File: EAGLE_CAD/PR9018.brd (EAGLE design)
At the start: 70 x 70 mm, 72 parts

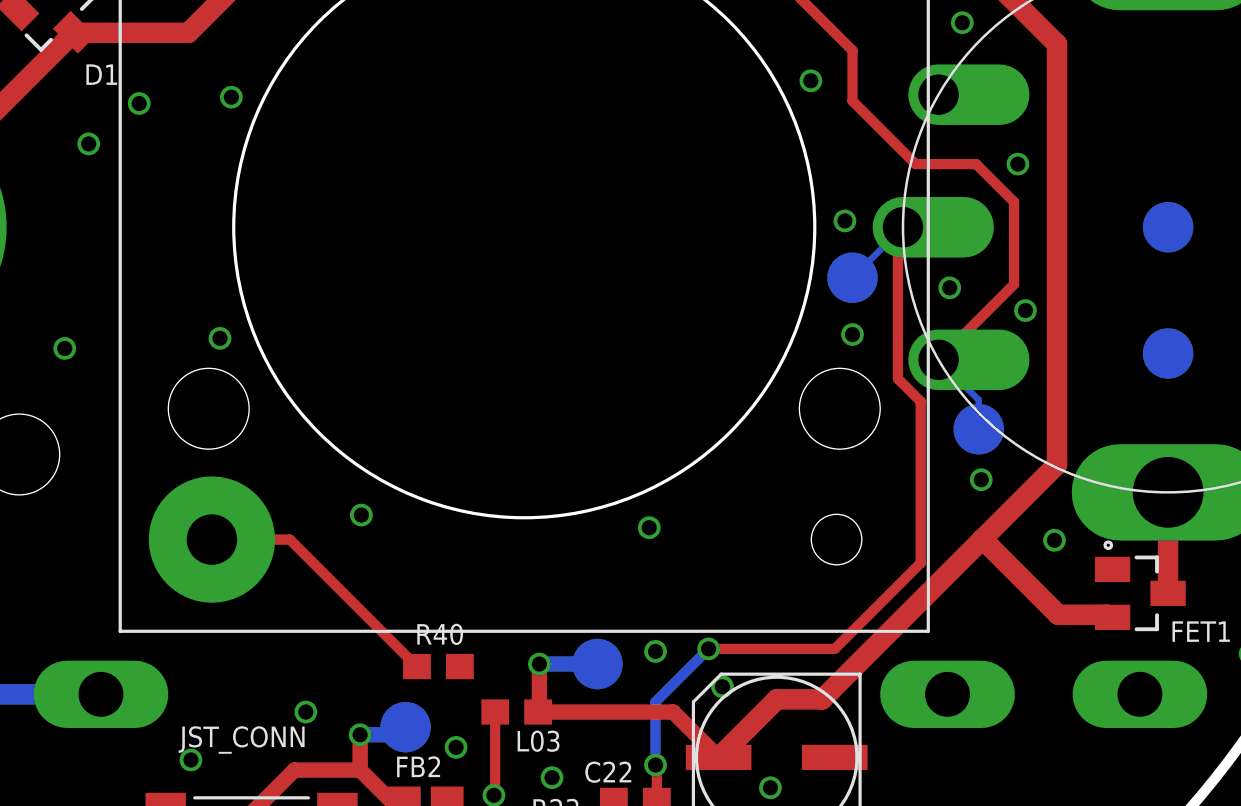
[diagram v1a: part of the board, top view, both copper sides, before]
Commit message: mostly speaker change
added big slot for wires
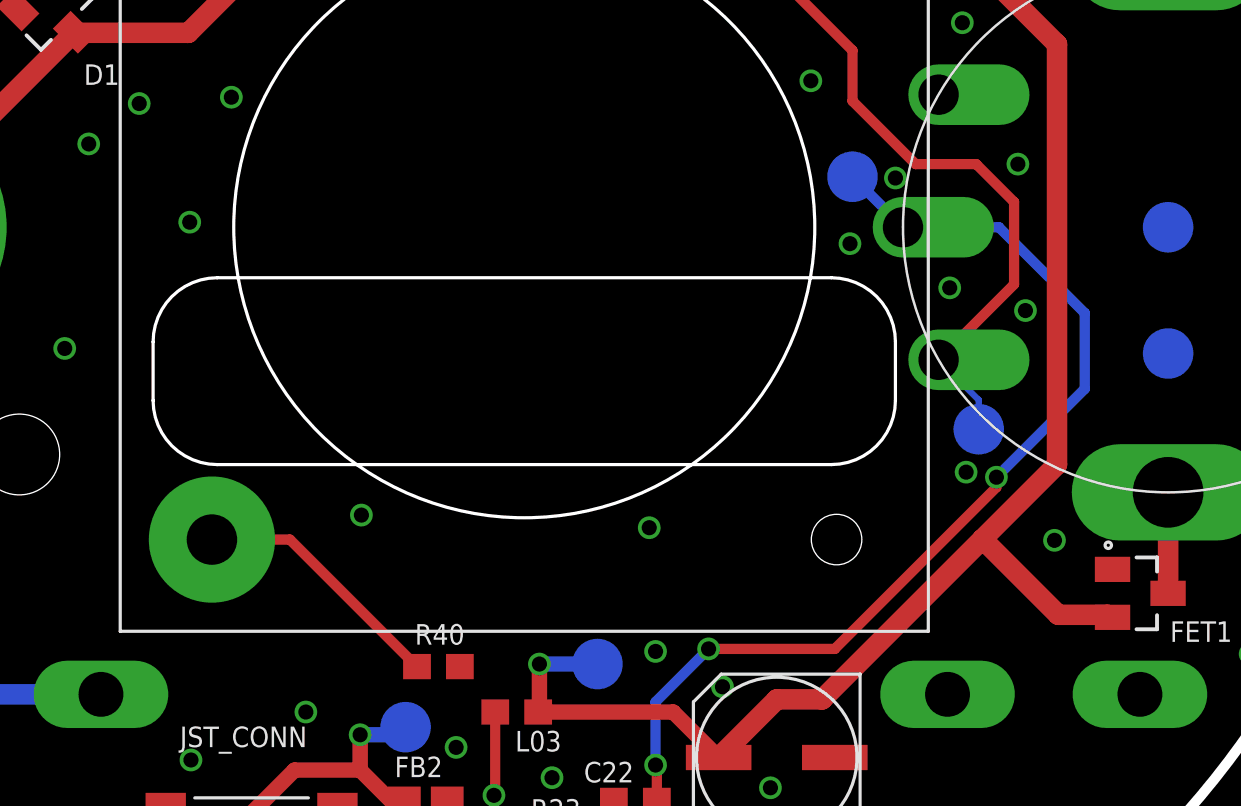
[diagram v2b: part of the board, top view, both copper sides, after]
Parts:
- moved TP17 4.00 mm to (48.0, 37.0)
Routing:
- net A_OUT: track 33.3 -> 40.7 mm, vias 2 -> 3
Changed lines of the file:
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@@
 <?xml version="1.0" encoding="utf-8"?>
 <!DOCTYPE eagle SYSTEM "eagle.dtd">
-<eagle version="6.6.0">
+<eagle version="7.2.0">
 <drawing>
 <settings>
@@
 <pass name="Default">
 <param name="RoutingGrid" value="50mil"/>
+<param name="AutoGrid" value="1"/>
+<param name="Efforts" value="0"/>
+<param name="TopRouterVariant" value="1"/>
 <param name="tpViaShape" value="round"/>
 <param name="PrefDir.1" value="|"/>
@@
 <attribute name="MFG_PN" value="DNP" x="53" y="27" size="1.778" layer="28" rot="MR0" display="off"/>
 </element>
-<element name="TP17" library="PR_Parts_Library" package="TP20R" value="" x="48" y="33" smashed="yes" rot="MR0">
-<attribute name="NAME" x="49" y="30.75" size="0.8128" layer="26" font="vector" ratio="16" rot="MR0"/>
-<attribute name="VALUE" x="48.762" y="31.984" size="0.0254" layer="28" rot="MR0"/>
-<attribute name="MFG_PN" value="DNP" x="48" y="33" size="1.778" layer="28" rot="MR0" display="off"/>
+<element name="TP17" library="PR_Parts_Library" package="TP20R" value="" x="48" y="37" smashed="yes" rot="MR0">
+<attribute name="NAME" x="49" y="34.75" size="0.8128" layer="26" font="vector" ratio="16" rot="MR0"/>
+<attribute name="VALUE" x="48.762" y="35.984" size="0.0254" layer="28" rot="MR0"/>
+<attribute name="MFG_PN" value="DNP" x="48" y="37" size="1.778" layer="28" rot="MR0" display="off"/>
 </element>
 <element name="C20" library="PR_Parts_Library" package="0603_CPL" value=".22uF" x="41.9" y="7.1" smashed="yes" rot="R180">
@@
 <via x="28.7" y="46.25" extent="1-16" drill="0.6"/>
 <via x="26.41" y="67.49" extent="1-16" drill="0.6"/>
-<via x="53.1" y="25" extent="1-16" drill="0.6"/>
+<via x="52.5" y="25.3" extent="1-16" drill="0.6"/>
 <via x="46.35" y="40.8" extent="1-16" drill="0.6"/>
 <via x="43.35" y="2.7" extent="1-16" drill="0.6"/>
@@
 <via x="54.7" y="62.45" extent="1-16" drill="0.5"/>
 <via x="39" y="59.45" extent="1-16" drill="0.6"/>
-<via x="47.7" y="35.25" extent="1-16" drill="0.6"/>
+<via x="49.7" y="36.95" extent="1-16" drill="0.6"/>
 <via x="23.3" y="56.9" extent="1-16" drill="0.6"/>
 <contactref element="FET1" pad="1"/>
@@
 <via x="19.75" y="39.9" extent="1-16" drill="0.6"/>
 <via x="23.4" y="40.15" extent="1-16" drill="0.6"/>
-<via x="22.95" y="30.6" extent="1-16" drill="0.6"/>
+<via x="21.75" y="35.2" extent="1-16" drill="0.6"/>
 <via x="34.9" y="48.05" extent="1-16" drill="0.6"/>
 <via x="16.7" y="62.95" extent="1-16" drill="0.6"/>
@@
 <via x="40.2" y="18.2" extent="1-16" drill="0.6"/>
 <via x="42.85" y="16.8" extent="1-16" drill="0.6"/>
-<via x="48" y="30.75" extent="1-16" drill="0.6"/>
+<via x="47.9" y="34.35" extent="1-16" drill="0.6"/>
 <via x="52.35" y="43.1" extent="1-16" drill="0.6"/>
 <via x="54.55" y="37.5" extent="1-16" drill="0.6"/>
@@
 <signal name="A_OUT">
 <contactref element="R1" pad="WIPER"/>
-<wire x1="49.8" y1="34.8" x2="50" y2="35" width="0.4064" layer="1"/>
-<wire x1="49.8" y1="34.8" x2="49.8" y2="29" width="0.4064" layer="1"/>
-<wire x1="49.8" y1="29" x2="50.7" y2="28.1" width="0.4064" layer="1"/>
-<wire x1="50.7" y1="28.1" x2="50.7" y2="21.7" width="0.4064" layer="1"/>
-<wire x1="50.7" y1="21.7" x2="47.3" y2="18.3" width="0.4064" layer="1"/>
 <wire x1="47.3" y1="18.3" x2="42.3" y2="18.3" width="0.4064" layer="1"/>
 <via x="42.3" y="18.3" extent="1-16" drill="0.6"/>
 <wire x1="42.3" y1="18.3" x2="40.2" y2="16.2" width="0.4064" layer="16"/>
 <contactref element="TP17" pad="TP"/>
-<wire x1="48" y1="33" x2="50" y2="35" width="0.254" layer="16"/>
 <contactref element="C22" pad="2"/>
 <wire x1="40.2" y1="16.2" x2="40.2" y2="13.7" width="0.4064" layer="16"/>
@@
 <wire x1="40.2" y1="13.7" x2="40.25" y2="13.65" width="0.4064" layer="1"/>
 <wire x1="40.25" y1="13.65" x2="40.25" y2="12.3" width="0.4064" layer="1"/>
+<wire x1="47.3" y1="18.3" x2="53.7" y2="24.7" width="0.4064" layer="1"/>
+<wire x1="53.7" y1="24.7" x2="53.7" y2="25.1" width="0.4064" layer="1"/>
+<via x="53.7" y="25.1" extent="1-16" drill="0.6"/>
+<wire x1="53.7" y1="25.1" x2="57.2" y2="28.6" width="0.4064" layer="16"/>
+<wire x1="57.2" y1="28.6" x2="57.2" y2="31.6" width="0.4064" layer="16"/>
+<wire x1="57.2" y1="31.6" x2="53.8" y2="35" width="0.4064" layer="16"/>
+<wire x1="53.8" y1="35" x2="50" y2="35" width="0.4064" layer="16"/>
+<wire x1="48" y1="37" x2="50" y2="35" width="0.4064" layer="16"/>
 </signal>
 <signal name="N$23">

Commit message: changed JST to top
and fucked with tnames a bunch
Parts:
- removed JST_CONN: (no value), PR_Parts_Library:JST-PH-2-SMT-RA
- added SPKR_PLUG: (no value), PR_Parts_Library:JST-B2B-PH-SM4-TB
- moved C21 2.57 mm to (41.9, 7.10)
- moved C20 1.20 mm to (41.9, 5.90)
- moved C22 0.45 mm to (39.2, 11.9), turned to 180 degrees
- moved R21 0.45 mm to (41.7, 8.70)
- moved R22 0.28 mm to (39.2, 10.7), turned to 0 degrees
- moved R20 0.20 mm to (38.7, 3.80)
- renumbered C01 to C1, C02 to C2, C03 to C3, C05 to C5, C08 to C8, L01 to L1, R02 to R2, R03 to R3, R04 to R4, R05 to R5, R07 to R7, R08 to R8, TP1 to T1, TP10 to T10, TP11 to T11, TP12 to T12, TP13 to T13, TP14 to T14, TP15 to T15, TP16 to T16, TP17 to T17, TP2 to T2, TP3 to T3, TP4 to T4, TP5 to T5, TP6 to T6, TP7 to T7, TP8 to T8, TP9 to T9
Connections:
- net SPK_OUT+: now also SPKR_PLUG.2; no longer JST_CONN.2
- net SPK_OUT-: now also SPKR_PLUG.1; no longer JST_CONN.1
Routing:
- net GND: track 21.1 -> 16.7 mm, vias 93 -> 102
- net N$14: track 5.30 -> 3.23 mm
- net SPK_OUT-: track 8.52 -> 10.3 mm
- net A_OUT: track 40.7 -> 42.1 mm
- net SPK_OUT+: track 17.8 -> 17.2 mm
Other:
- outline, holes or cut-outs redrawn

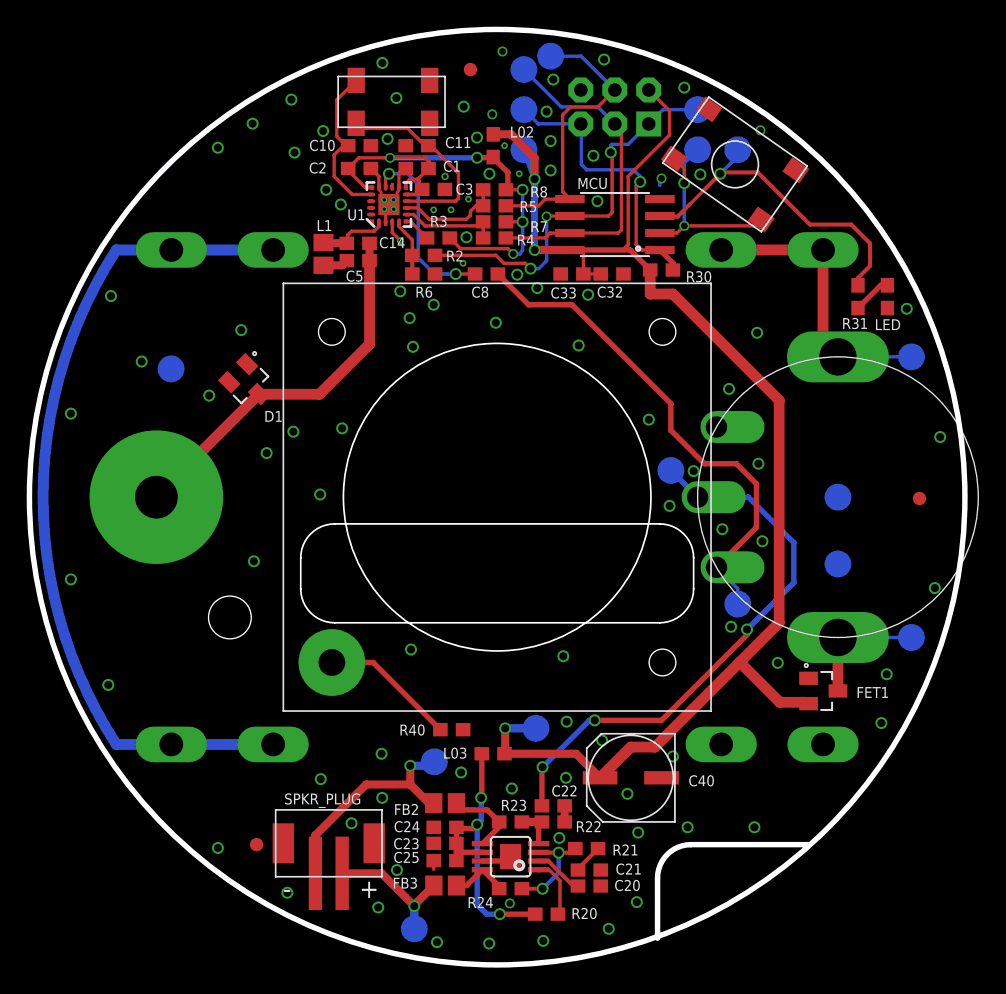
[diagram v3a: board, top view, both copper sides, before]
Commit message: mostly test points and logo
moved test points so that they can be accessed with batteries in

made a logo package and added that to the layout

moved some small stuff around
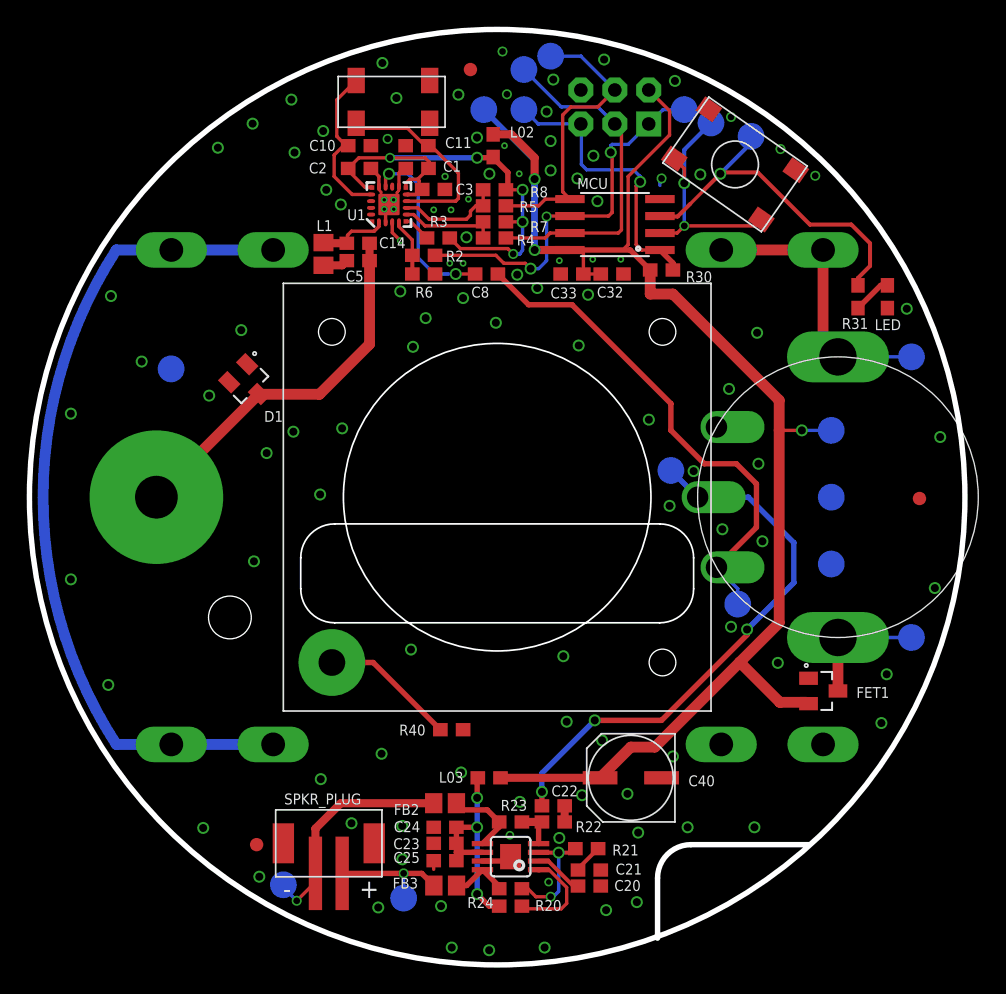
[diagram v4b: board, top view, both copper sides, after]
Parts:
- added U$1: (no value), PR_Parts_Library:PR_LOGO
- moved T4 31.4 mm to (60.0, 40.0)
- moved T6 14.6 mm to (19.0, 6.00)
- moved T5 4.24 mm to (34.0, 64.0)
- moved R20 2.77 mm to (36.0, 4.40)
- moved T7 2.44 mm to (28.0, 5.00)
- moved T8 2.24 mm to (51.0, 63.0)
- moved L03 1.82 mm to (34.4, 14.0)
- moved T9 1.41 mm to (54.0, 62.0)
- moved T10 1.00 mm to (49.0, 64.0)
- moved T2 0.50 mm to (60.0, 35.0)
- moved T3 0.50 mm to (60.0, 30.0)
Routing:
- net N$2: track 22.6 -> 16.7 mm
- net VCC: track 110.7 -> 114.3 mm
- net N$20: track 4.50 -> 7.45 mm
- net SW: track 16.3 -> 18.7 mm
- net LED/PB4: track 25.4 -> 26.8 mm
- net N$5: track 7.63 -> 8.95 mm
- net SPK_OUT-: track 10.3 -> 9.09 mm
- net !RST: track 30.0 -> 29.0 mm
- net GND: vias 102 -> 111

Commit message: Text and DRC
Text and DRC
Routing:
- net VCC: track 114.3 -> 115.0 mm
- net GND: vias 111 -> 112
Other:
- board text added: "Brooklyn, NY By Centerline Labs"
- board text removed: "Board # PR9017 DVT/DFM Pre-production"
